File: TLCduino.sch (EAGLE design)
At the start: 33 parts

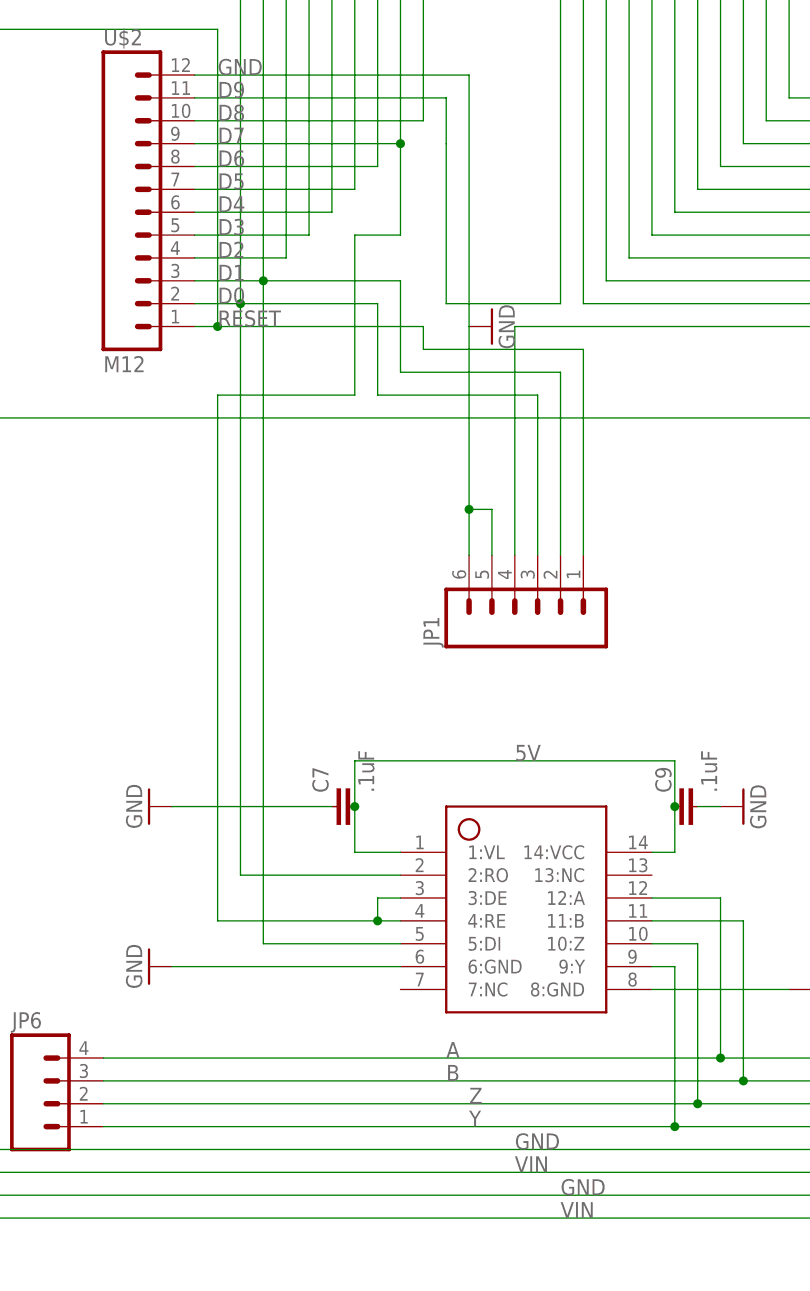
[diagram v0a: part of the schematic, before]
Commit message: Major revision, on board jacks, other revisions to address weaknesses discovered in actual use.
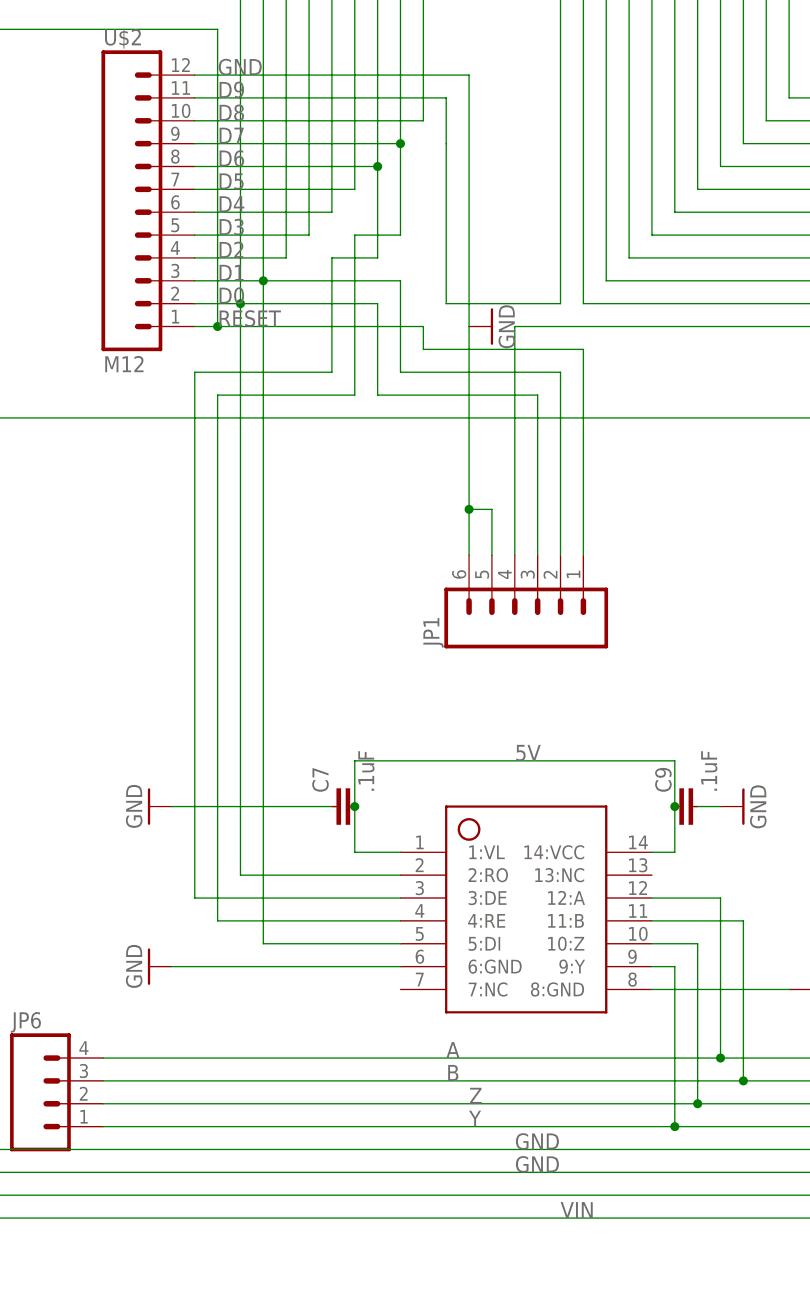
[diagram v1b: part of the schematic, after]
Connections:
- net D6: now also U$6.3:DE
- net D7: no longer U$6.3:DE
- net GND: now also JP7.3, JP9.2; no longer JP7.2, JP9.3
- net VIN: now also JP7.2, JP9.3; no longer JP7.3, JP9.2
